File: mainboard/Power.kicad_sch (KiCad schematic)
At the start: 34 parts, among them IC801 LP5907MFX-2.8, IC802 LP5907MFX-1.5, IC803 TPS62823DLC, IC804 LP5907MFX-3.0, IC805 LP5907MFX-2.8, IC806 LP5907MFX-1.2, SW801 On / Off

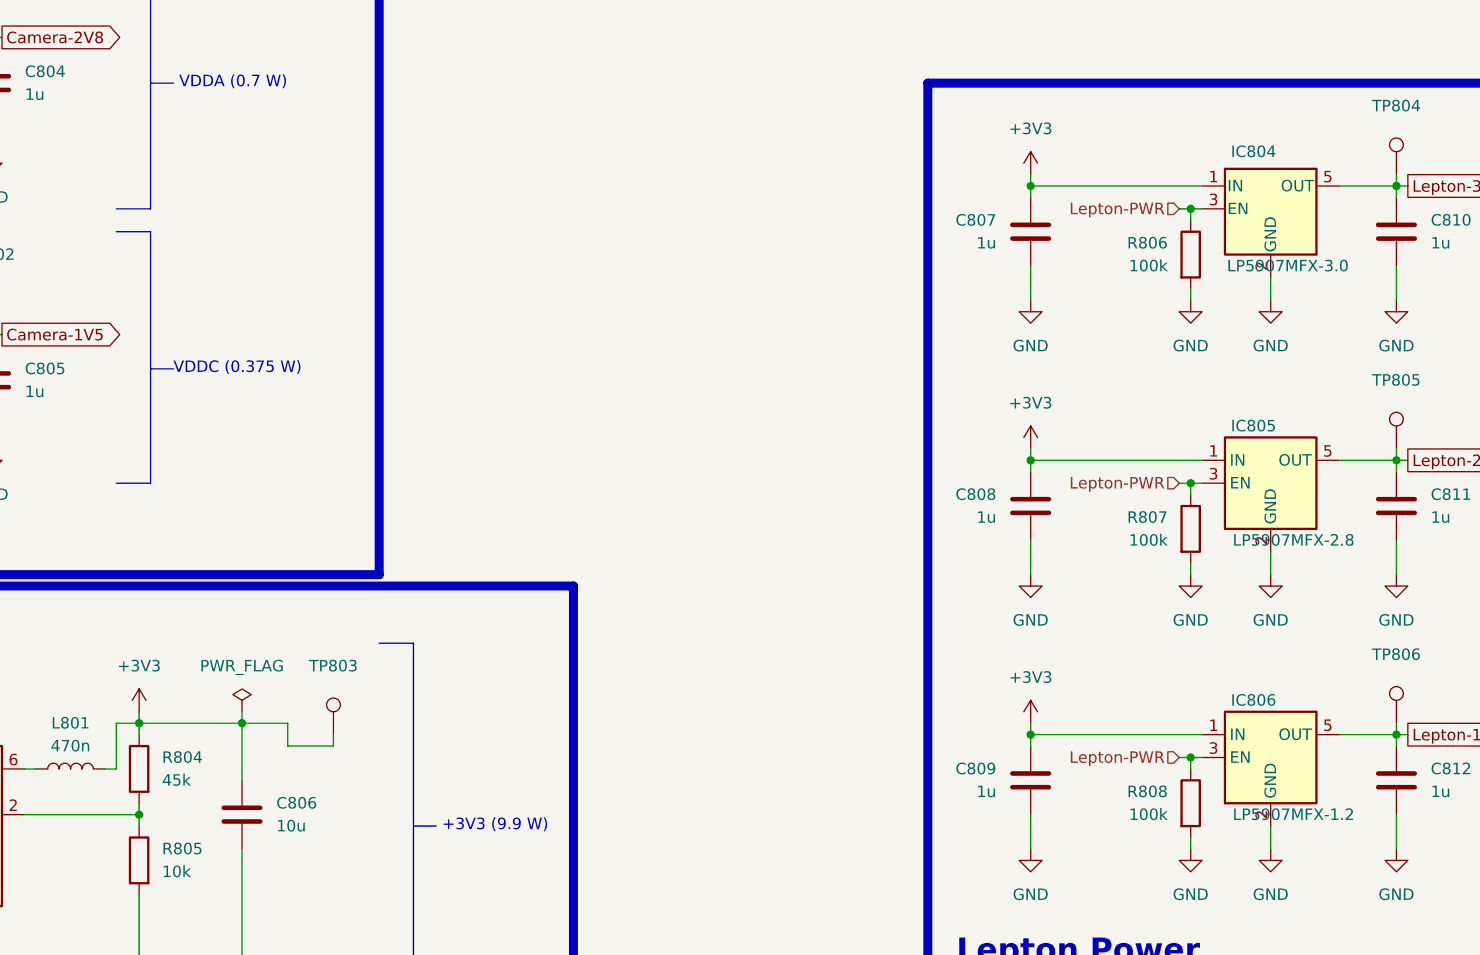
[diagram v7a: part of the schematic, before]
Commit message: Prepare release 1.0.2
Signed-off-by: Daniel Kampert <DanielKampert@kampis-elektroecke.de>
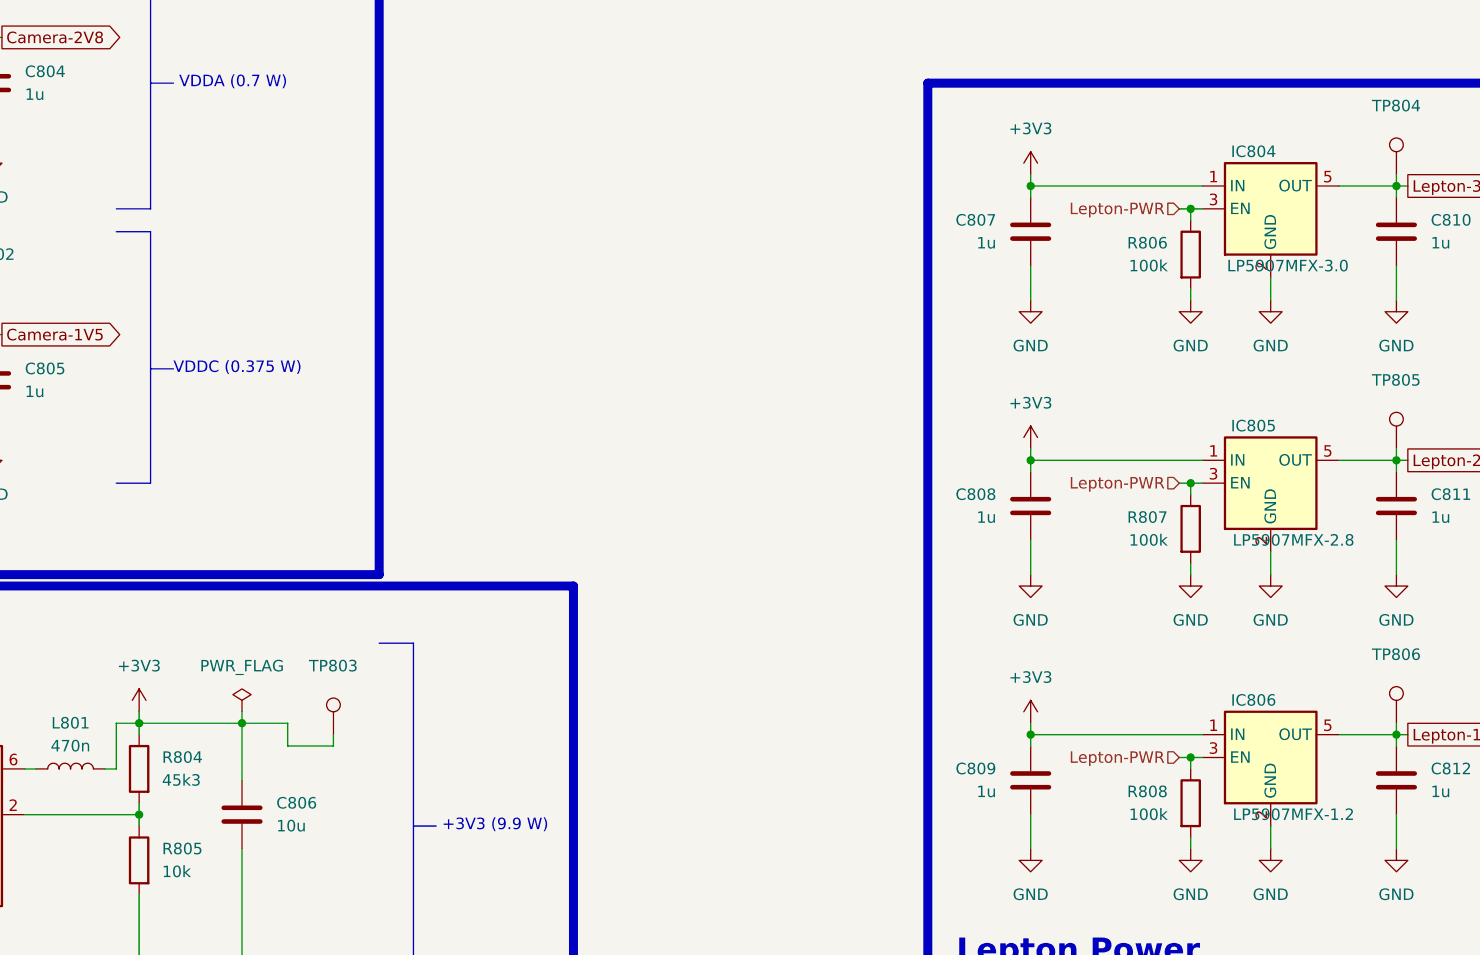
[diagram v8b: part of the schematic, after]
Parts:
- IC804: symbol Regulator_Linear:TLV75530PDBV -> Regulator_Linear:LP5907MFX-3.0
- R804: value 45k -> 45k3
- R805: manf# RC0603FR-073K3L -> RC0603FR-0710KL; mouser# 603-RC0603FR-073K3L -> 603-RC0603FR-0710KL
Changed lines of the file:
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@@
 			)
 		)
-		(property "Value" "45k"
+		(property "Value" "45k3"
 			(at 87.63 118.11 0)
 			(effects
@@
 	)
 	(symbol
-		(lib_id "Regulator_Linear:TLV75530PDBV")
+		(lib_id "Regulator_Linear:LP5907MFX-3.0")
 		(at 210.82 54.61 0)
 		(unit 1)
@@
 		)
 		(property "Footprint" "Package_TO_SOT_SMD:SOT-23-5"
-			(at 210.82 46.355 0)
+			(at 210.82 45.72 0)
 			(effects
 				(font
 					(size 1.27 1.27)
-					(italic yes)
 				)
 				(hide yes)
 			)
 		)
-		(property "Datasheet" "http://www.ti.com/lit/ds/symlink/tlv755p.pdf"
-			(at 210.82 53.34 0)
+		(property "Datasheet" "http://www.ti.com/lit/ds/symlink/lp5907.pdf"
+			(at 210.82 41.91 0)
 			(effects
 				(font
@@
 			)
 		)
-		(property "Description" "500mA Low Dropout Voltage Regulator, Fixed Output 3.0V, SOT-23-5"
+		(property "Description" "250-mA Ultra-Low-Noise Low-IQ LDO, 3.0V, SOT-23"
 			(at 210.82 54.61 0)
 			(effects
@@
 			)
 		)
-		(property "manf#" "RC0603FR-073K3L"
+		(property "manf#" "RC0603FR-0710KL"
 			(at 85.09 127 0)
 			(effects
@@
 			)
 		)
-		(property "mouser#" "603-RC0603FR-073K3L"
+		(property "mouser#" "603-RC0603FR-0710KL"
 			(at 85.09 127 0)
 			(effects
